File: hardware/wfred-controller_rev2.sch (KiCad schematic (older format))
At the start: 11 parts, among them IC201 ATMEGA32-A, P201 ISP, X201 14.7456MHz

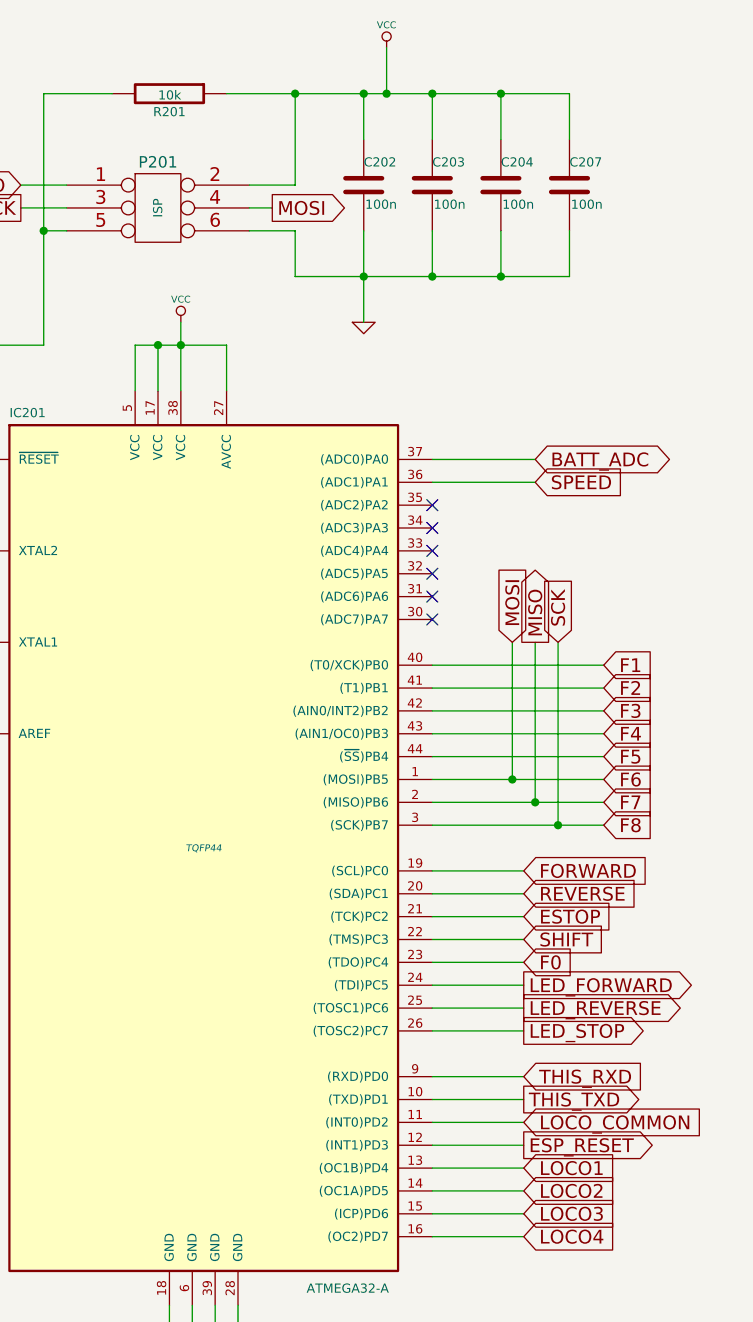
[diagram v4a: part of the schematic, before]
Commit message: Changed power concept (again)
- Exchanged regulator for one with lower shutdown current
- Moved AVR directly to battery
- Added voltage regulator enable connection to AVR
- Added Speed potentiometer power supply from AVR

New power concept: AVR stays always-on (POWER DOWN MODE if not in use)
and shuts down speed potentiometer and ESP8266 when idle or battery low
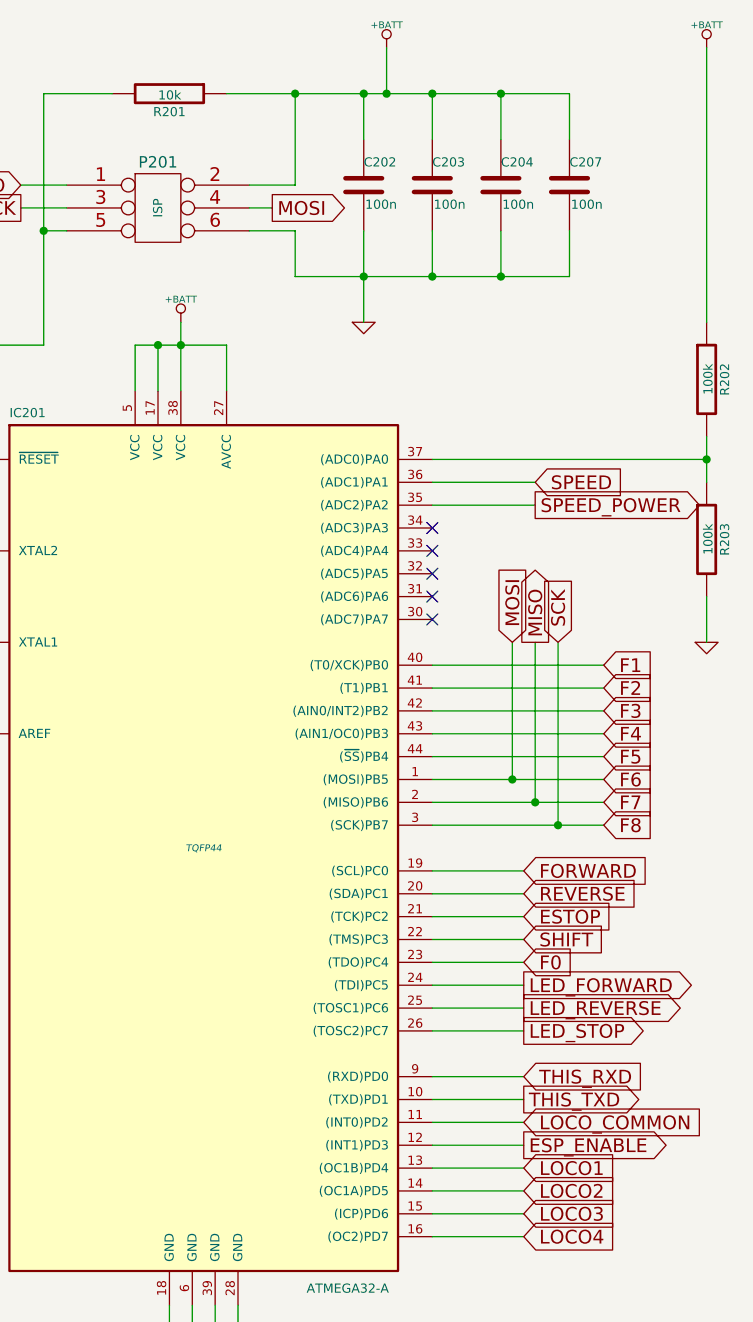
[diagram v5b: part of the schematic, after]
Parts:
- added R202, R203: 100k, symbol R
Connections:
- net GND: now also R203.2
- net SPEED_POWER: now reaches IC201.35 ((ADC2)PA2)
- net BATT_ADC: no longer names the net of IC201.37 ((ADC0)PA0)
- net BATT_ADC: now also R202.2, R203.1
- net ESP_RESET renamed ESP_ENABLE
- net VCC renamed +BATT
- net +BATT: now also R202.1
- no-connect marks 6 -> 5
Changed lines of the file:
@@
 LIBS:LDL1117S30R
 LIBS:MCP73831T-2ACI_OT
+LIBS:NCV8161BSN300T1G
 LIBS:wfred_rev2-cache
 EELAYER 25 0
@@
 MOSI
 $Comp
-L PWR_FLAG #FLG025
+L PWR_FLAG #FLG026
 U 1 1 59214642
 P 2500 4300
-F 0 "#FLG025" H 2500 4395 30  0001 C CNN
+F 0 "#FLG026" H 2500 4395 30  0001 C CNN
 F 1 "PWR_FLAG" H 2500 4480 30  0000 C CNN
 F 2 "" H 2500 4300 60  0001 C CNN
@@
 $EndComp
 $Comp
-L GND-RESCUE-wfred_rev2 #PWR026
+L GND-RESCUE-wfred_rev2 #PWR027
 U 1 1 5920D54C
 P 1700 4200
-F 0 "#PWR026" H 1700 4200 30  0001 C CNN
+F 0 "#PWR027" H 1700 4200 30  0001 C CNN
 F 1 "GND" H 1700 4130 30  0001 C CNN
 F 2 "" H 1700 4200 60  0001 C CNN
@@
 $EndComp
 $Comp
-L GND-RESCUE-wfred_rev2 #PWR027
+L GND-RESCUE-wfred_rev2 #PWR028
 U 1 1 5920D60E
 P 5300 2600
-F 0 "#PWR027" H 5300 2600 30  0001 C CNN
+F 0 "#PWR028" H 5300 2600 30  0001 C CNN
 F 1 "GND" H 5300 2530 30  0001 C CNN
 F 2 "" H 5300 2600 60  0001 C CNN
 F 3 "" H 5300 2600 60  0001 C CNN
 	1    5300 2600
-	1    0    0    -1
-$EndComp
-$Comp
-L VCC #PWR028
-U 1 1 5920D930
-P 5400 1400
-F 0 "#PWR028" H 5400 1500 30  0001 C CNN
-F 1 "VCC" H 5400 1500 30  0000 C CNN
-F 2 "" H 5400 1400 60  0001 C CNN
-F 3 "" H 5400 1400 60  0001 C CNN
-	1    5400 1400
 	1    0    0    -1
 $EndComp
@@
 	1    0    0    -1
 $EndComp
-Text GLabel 6050 3200 2    60   BiDi ~ 0
-BATT_ADC
 $Comp
 L ATMEGA32-A IC201
@@
 F 3 "" H 4600 4900 60  0001 C CNN
 	1    4600 4900
-	1    0    0    -1
-$EndComp
-$Comp
-L VCC #PWR033
-U 1 1 5BDF8EC5
-P 4500 2600
-F 0 "#PWR033" H 4500 2700 30  0001 C CNN
-F 1 "VCC" H 4500 2700 30  0000 C CNN
-F 2 "" H 4500 2600 60  0001 C CNN
-F 3 "" H 4500 2600 60  0001 C CNN
-	1    4500 2600
 	1    0    0    -1
 $EndComp
@@
 	5600 6100 6000 6100
 Wire Wire Line
-	5600 3200 6050 3200
-Wire Wire Line
 	6050 3300 5600 3300
 Wire Wire Line
@@
 Wire Wire Line
 	5600 5600 6000 5600
-NoConn ~ 5600 3400
 NoConn ~ 5600 3500
 NoConn ~ 5600 3600
@@
 	3900 2200 4000 2200
 Text GLabel 6000 6200 2    60   Output ~ 0
-ESP_RESET
+ESP_ENABLE
 Wire Wire Line
 	5600 6200 6000 6200
+$Comp
+L +BATT #PWR033
+U 1 1 5BE0AEFB
+P 5400 1400
+F 0 "#PWR033" H 5400 1350 20  0001 C CNN
+F 1 "+BATT" H 5400 1500 30  0000 C CNN
+F 2 "" H 5400 1400 60  0001 C CNN
+F 3 "" H 5400 1400 60  0001 C CNN
+	1    5400 1400
+	1    0    0    -1
+$EndComp
+$Comp
+L +BATT #PWR034
+U 1 1 5BE0AF30
+P 4500 2600
+F 0 "#PWR034" H 4500 2550 20  0001 C CNN
+F 1 "+BATT" H 4500 2700 30  0000 C CNN
+F 2 "" H 4500 2600 60  0001 C CNN
+F 3 "" H 4500 2600 60  0001 C CNN
+	1    4500 2600
+	1    0    0    -1
+$EndComp
+$Comp
+L R R202
+U 1 1 5BE0AFE0
+P 6800 2850
+F 0 "R202" V 6880 2850 40  0000 C CNN
+F 1 "100k" V 6807 2851 40  0000 C CNN
+F 2 "" V 6730 2850 30  0000 C CNN
+F 3 "" H 6800 2850 30  0000 C CNN
+	1    6800 2850
+	1    0    0    -1
+$EndComp
+$Comp
+L R R203
+U 1 1 5BE0B09F
+P 6800 3550
+F 0 "R203" V 6880 3550 40  0000 C CNN
+F 1 "100k" V 6807 3551 40  0000 C CNN
+F 2 "" V 6730 3550 30  0000 C CNN
+F 3 "" H 6800 3550 30  0000 C CNN
+	1    6800 3550
+	1    0    0    -1
+$EndComp
+Wire Wire Line
+	5600 3200 6800 3200
+Wire Wire Line
+	6800 3100 6800 3300
+Connection ~ 6800 3200
+$Comp
+L +BATT #PWR035
+U 1 1 5BE0B208
+P 6800 1400
+F 0 "#PWR035" H 6800 1350 20  0001 C CNN
+F 1 "+BATT" H 6800 1500 30  0000 C CNN
+F 2 "" H 6800 1400 60  0001 C CNN
+F 3 "" H 6800 1400 60  0001 C CNN
+	1    6800 1400
+	1    0    0    -1
+$EndComp
+Wire Wire Line
+	6800 1400 6800 2600
+$Comp
+L GND-RESCUE-wfred_rev2 #PWR036
+U 1 1 5BE0B2E4
+P 6800 4000
+F 0 "#PWR036" H 6800 4000 30  0001 C CNN
+F 1 "GND" H 6800 3930 30  0001 C CNN
+F 2 "" H 6800 4000 60  0001 C CNN
+F 3 "" H 6800 4000 60  0001 C CNN
+	1    6800 4000
+	1    0    0    -1
+$EndComp
+Wire Wire Line
+	6800 4000 6800 3800
+Text GLabel 6050 3400 2    60   Output ~ 0
+SPEED_POWER
+Wire Wire Line
+	5600 3400 6050 3400
 $EndSCHEMATC

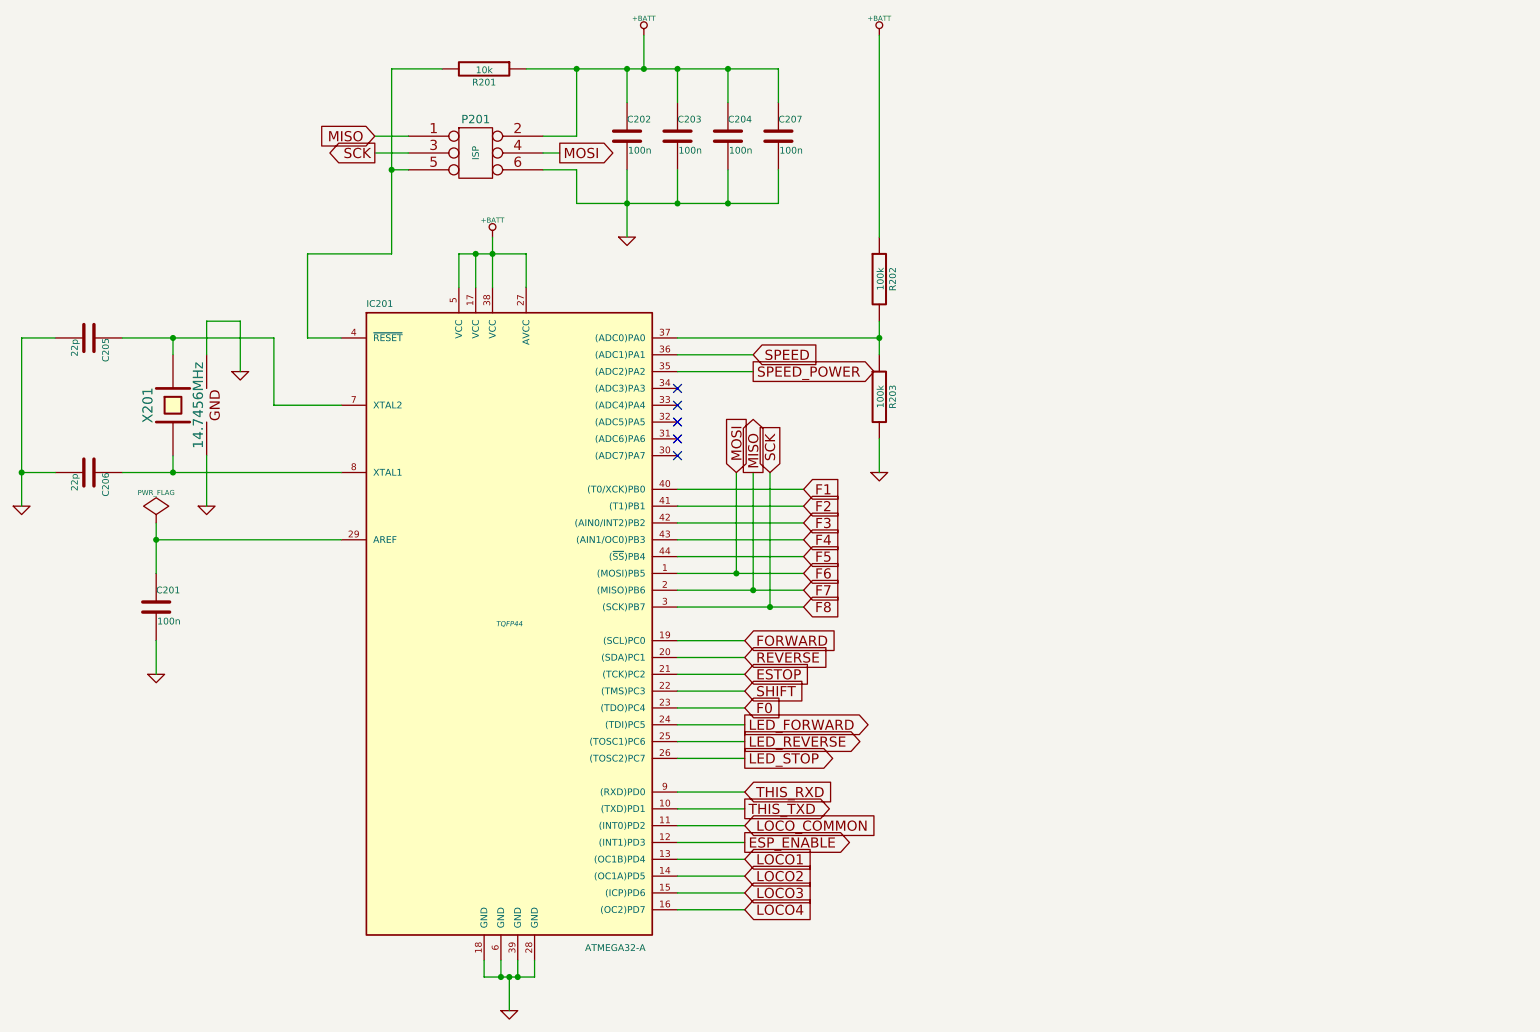
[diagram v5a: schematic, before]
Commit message: First PCB draft for LiPo version
- Returned to ATMega328 / not enough space for ATMega32
- Moved to multiplexing key and direction inputs -> kept F5-F8
- Most traces are now 0.5mm wide
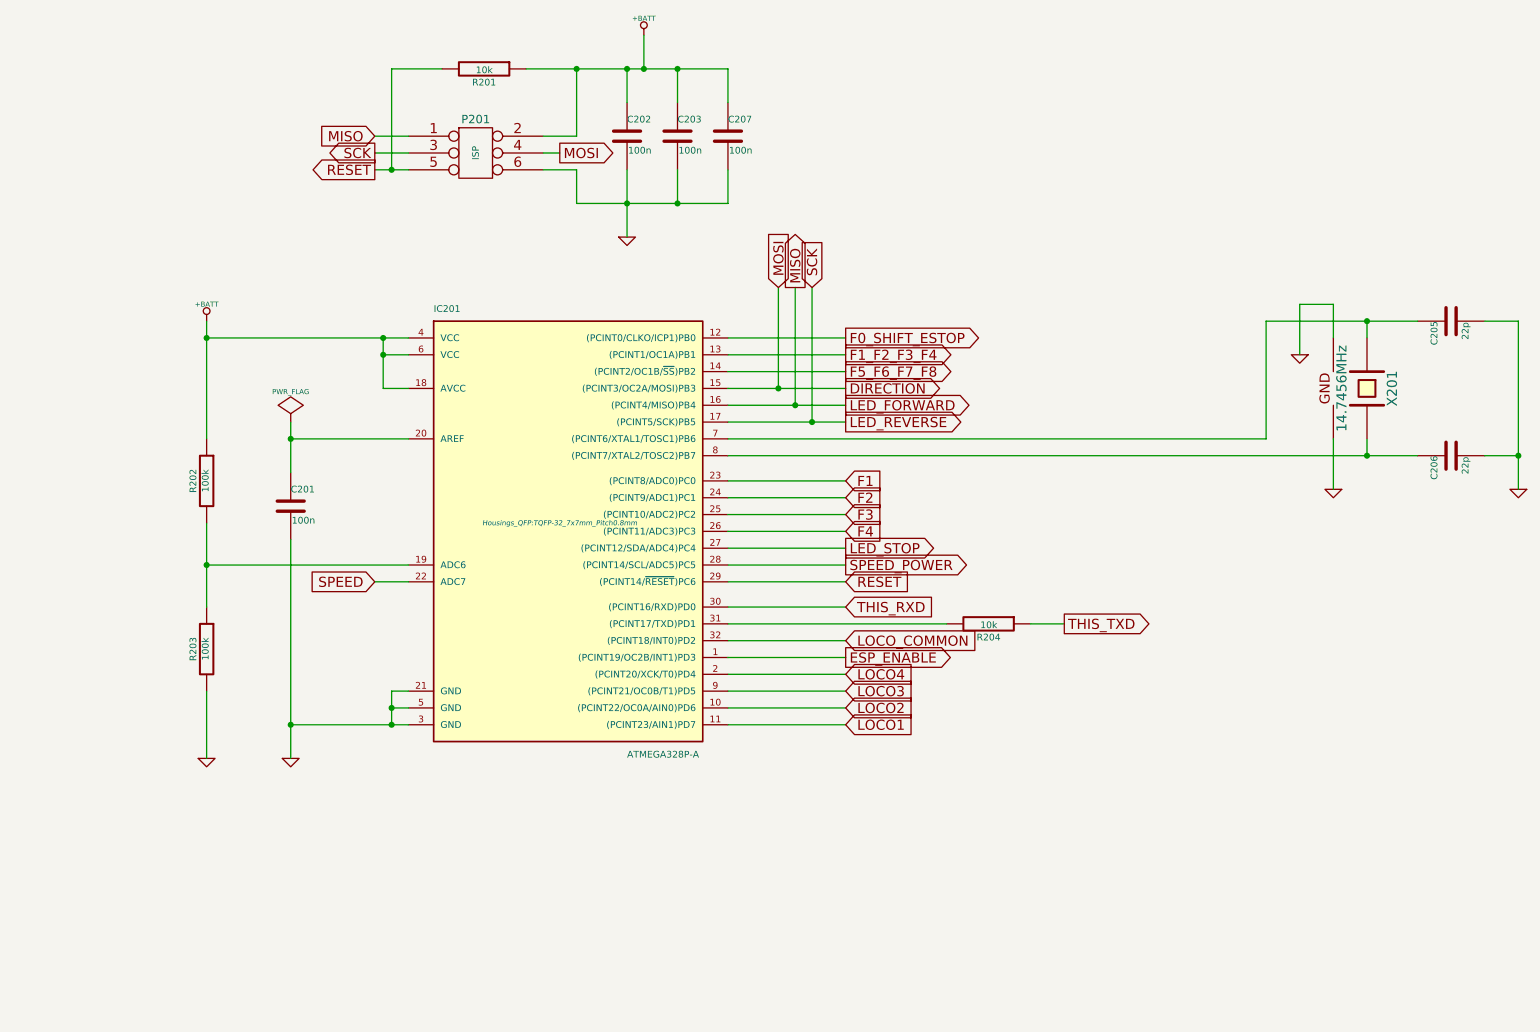
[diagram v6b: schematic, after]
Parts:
- removed C204: 100n, Capacitors_SMD:C_0805_HandSoldering, symbol C-RESCUE-wfred_rev2
- removed IC201: ATMEGA32-A, TQFP44, symbol ATMEGA32-A
- added IC201: ATMEGA328P-A, Housings_QFP:TQFP-32_7x7mm_Pitch0.8mm, symbol ATMEGA328P-A
- added R204: 10k, Capacitors_SMD:C_0805_HandSoldering, symbol R
- P201: footprint Pin_Headers:Pin_Header_Straight_2x03_Pitch2.54mm -> Pin_Headers:Pin_Header_Straight_2x03_Pitch2.54mm_SMD
- R202, R203: footprint (none) -> Capacitors_SMD:C_0805_HandSoldering
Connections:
- net F7 is gone; now on net LED_FORWARD: P201.1
- net F8 is gone; now on net LED_REVERSE: P201.3
- net +BATT: now also IC201.18 (AVCC), IC201.4 (VCC), IC201.6 (VCC)
- net ESP_ENABLE: now also IC201.1 ((PCINT19/OC2B/INT1)PD3)
- net F1: now also IC201.23 ((PCINT8/ADC0)PC0)
- net F2: now also IC201.24 ((PCINT9/ADC1)PC1)
- net F3: now also IC201.25 ((PCINT10/ADC2)PC2)
- net F4: now also IC201.26 ((PCINT11/ADC3)PC3)
- net GND: now also IC201.21 (GND), IC201.3 (GND), IC201.5 (GND)
- net LED_FORWARD: now also IC201.16 ((PCINT4/MISO)PB4)
- net LED_REVERSE: now also IC201.17 ((PCINT5/SCK)PB5)
- net LED_STOP: now also IC201.27 ((PCINT12/SDA/ADC4)PC4)
- net LOCO1: now also IC201.11 ((PCINT23/AIN1)PD7)
- net LOCO2: now also IC201.10 ((PCINT22/OC0A/AIN0)PD6)
- net LOCO3: now also IC201.9 ((PCINT21/OC0B/T1)PD5)
- net LOCO4: now also IC201.2 ((PCINT20/XCK/T0)PD4)
- net LOCO_COMMON: now also IC201.32 ((PCINT18/INT0)PD2)
- net SPEED: now also IC201.22 (ADC7)
- net SPEED_POWER: now also IC201.28 ((PCINT14/SCL/ADC5)PC5)
- net THIS_RXD: now also IC201.30 ((PCINT16/RXD)PD0)
- net THIS_TXD: now also R204.1
- net at C205.1, X201.1: now also IC201.7 ((PCINT6/XTAL1/TOSC1)PB6)
- net at C206.1, X201.3: now also IC201.8 ((PCINT7/XTAL2/TOSC2)PB7)
- net at C201.1: now also IC201.20 (AREF)
- net RESET: now reaches P201.5, R201.2
- net RESET: now also IC201.29 ((PCINT14/~RESET~)PC6)
- net at R202.2, R203.1: now also IC201.19 (ADC6)
- net F6 renamed DIRECTION
- net DIRECTION: now also IC201.15 ((PCINT3/OC2A/MOSI)PB3)
- new net: IC201.31 ((PCINT17/TXD)PD1), R204.2
- new net F0_SHIFT_ESTOP: IC201.12 ((PCINT0/CLKO/ICP1)PB0)
- new net F1_F2_F3_F4: IC201.13 ((PCINT1/OC1A)PB1)
- new net F5_F6_F7_F8: IC201.14 ((PCINT2/OC1B/~SS~)PB2)
- no-connect marks 5 -> 0
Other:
- moved on the sheet: C201, C205, C206, C207, R202, R203, X201

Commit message: Changed schematic to AA batteries and holder
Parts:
- removed R204: 10k, Capacitors_SMD:C_0805_HandSoldering, symbol R
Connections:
- net +BATT: no longer C202.1, C203.1, C207.1, P201.2, R201.1
- net THIS_TXD: now also IC201.31 ((PCINT17/TXD)PD1)
- new net VCC: C202.1, C203.1, C207.1, P201.2, R201.1
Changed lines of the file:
@@
 LIBS:my_devices
 LIBS:ESP8266
-LIBS:LDL1117S30R
-LIBS:MCP73831T-2ACI_OT
-LIBS:NCV8161BSN300T1G
 LIBS:wfred_rev2-cache
 EELAYER 25 0
@@
 MOSI
 $Comp
-L PWR_FLAG #FLG026
+L PWR_FLAG #FLG013
 U 1 1 59214642
 P 3300 3700
-F 0 "#FLG026" H 3300 3795 30  0001 C CNN
+F 0 "#FLG013" H 3300 3795 30  0001 C CNN
 F 1 "PWR_FLAG" H 3300 3880 30  0000 C CNN
 F 2 "" H 3300 3700 60  0001 C CNN
@@
 $EndComp
 $Comp
-L GND-RESCUE-wfred_rev2 #PWR027
+L GND-RESCUE-wfred_rev2 #PWR014
 U 1 1 5920D54C
 P 10600 4100
-F 0 "#PWR027" H 10600 4100 30  0001 C CNN
+F 0 "#PWR014" H 10600 4100 30  0001 C CNN
 F 1 "GND" H 10600 4030 30  0001 C CNN
 F 2 "" H 10600 4100 60  0001 C CNN
@@
 $EndComp
 $Comp
-L GND-RESCUE-wfred_rev2 #PWR028
+L GND-RESCUE-wfred_rev2 #PWR015
 U 1 1 5920D60E
 P 5300 2600
-F 0 "#PWR028" H 5300 2600 30  0001 C CNN
+F 0 "#PWR015" H 5300 2600 30  0001 C CNN
 F 1 "GND" H 5300 2530 30  0001 C CNN
 F 2 "" H 5300 2600 60  0001 C CNN
@@
 	1    0    0    -1
 $EndComp
-Text GLabel 7900 4900 2    60   Output ~ 0
+Text GLabel 6600 4900 2    60   Output ~ 0
 THIS_TXD
 Text GLabel 6600 4800 2    60   Input ~ 0
@@
 LED_FORWARD
 $Comp
-L GND-RESCUE-wfred_rev2 #PWR029
+L GND-RESCUE-wfred_rev2 #PWR016
 U 1 1 592F4690
 P 3300 5700
-F 0 "#PWR029" H 3300 5700 30  0001 C CNN
+F 0 "#PWR016" H 3300 5700 30  0001 C CNN
 F 1 "GND" H 3300 5630 30  0001 C CNN
 F 2 "" H 3300 5700 60  0001 C CNN
@@
 $EndComp
 $Comp
-L GND-RESCUE-wfred_rev2 #PWR030
+L GND-RESCUE-wfred_rev2 #PWR017
 U 1 1 5A171EC6
 P 9500 4100
-F 0 "#PWR030" H 9500 4100 30  0001 C CNN
+F 0 "#PWR017" H 9500 4100 30  0001 C CNN
 F 1 "GND" H 9500 4030 30  0001 C CNN
 F 2 "" H 9500 4100 60  0001 C CNN
@@
 $EndComp
 $Comp
-L GND-RESCUE-wfred_rev2 #PWR031
+L GND-RESCUE-wfred_rev2 #PWR018
 U 1 1 5A171EEF
 P 9300 3300
-F 0 "#PWR031" H 9300 3300 30  0001 C CNN
+F 0 "#PWR018" H 9300 3300 30  0001 C CNN
 F 1 "GND" H 9300 3230 30  0001 C CNN
 F 2 "" H 9300 3300 60  0001 C CNN
@@
 ESP_ENABLE
 $Comp
-L +BATT #PWR032
-U 1 1 5BE0AEFB
-P 5400 1400
-F 0 "#PWR032" H 5400 1350 20  0001 C CNN
-F 1 "+BATT" H 5400 1500 30  0000 C CNN
-F 2 "" H 5400 1400 60  0001 C CNN
-F 3 "" H 5400 1400 60  0001 C CNN
-	1    5400 1400
-	1    0    0    -1
-$EndComp
-$Comp
 L R R202
 U 1 1 5BE0AFE0
@@
 $EndComp
 $Comp
-L +BATT #PWR033
+L +BATT #PWR019
 U 1 1 5BE0B208
 P 2800 3100
-F 0 "#PWR033" H 2800 3050 20  0001 C CNN
+F 0 "#PWR019" H 2800 3050 20  0001 C CNN
 F 1 "+BATT" H 2800 3200 30  0000 C CNN
 F 2 "" H 2800 3100 60  0001 C CNN
@@
 Text GLabel 6600 4550 2    60   Output ~ 0
 SPEED_POWER
-$Comp
-L R R204
-U 1 1 5BE0AFA5
-P 7450 4900
-F 0 "R204" V 7530 4900 40  0000 C CNN
-F 1 "10k" V 7457 4901 40  0000 C CNN
-F 2 "Capacitors_SMD:C_0805_HandSoldering" V 7380 4900 30  0001 C CNN
-F 3 "" H 7450 4900 30  0000 C CNN
-	1    7450 4900
-	0    1    1    0
-$EndComp
 Wire Wire Line
 	9700 3100 9700 3200
@@
 	5900 4800 6600 4800
 Wire Wire Line
-	5900 4900 7200 4900
+	5900 4900 6600 4900
 Wire Wire Line
 	3900 1600 3900 2200
@@
 Wire Wire Line
 	5900 4550 6600 4550
-Wire Wire Line
-	7700 4900 7900 4900
 $Comp
 L ATMEGA328P-A IC201
@@
 Connection ~ 3850 3300
 $Comp
-L GND-RESCUE-wfred_rev2 #PWR034
+L GND-RESCUE-wfred_rev2 #PWR020
 U 1 1 5BE232F3
 P 2800 5700
-F 0 "#PWR034" H 2800 5700 30  0001 C CNN
+F 0 "#PWR020" H 2800 5700 30  0001 C CNN
 F 1 "GND" H 2800 5630 30  0001 C CNN
 F 2 "" H 2800 5700 60  0001 C CNN
@@
 	3800 4650 4000 4650
 Connection ~ 2800 4550
+$Comp
+L VCC #PWR021
+U 1 1 5BE4849E
+P 5400 1400
+F 0 "#PWR021" H 5400 1500 30  0001 C CNN
+F 1 "VCC" H 5400 1500 30  0000 C CNN
+F 2 "" H 5400 1400 60  0001 C CNN
+F 3 "" H 5400 1400 60  0001 C CNN
+	1    5400 1400
+	1    0    0    -1
+$EndComp
 $EndSCHEMATC
